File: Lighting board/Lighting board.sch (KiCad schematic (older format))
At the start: 16 parts, among them SW1 SW_SPDT, U1 LDD-1500L, U2 LDD-1500L, U3 TM4C129E_Launchpad, U4 OKI

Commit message: PDR commit
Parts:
- removed C2: 10uF, Capacitor_SMD:C_0603_1608Metric_Pad1.05x0.95mm_HandSolder, symbol Device:C
- removed Conn2C2: Molex_SL_03, MRDT_Connectors:MOLEX_SL_03_Vertical, symbol MRDT_Connectors:Molex_SL_03
- removed R2: 1k, Resistor_SMD:R_0603_1608Metric_Pad1.05x0.95mm_HandSolder, symbol Device:R
- Conn1C1, Conn1D1: footprint MRDT_Connectors:MOLEX_SL_02_Vertical -> MRDT_Connectors:MOLEX_SL_02_Horizontal
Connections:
- net labels removed: Dout_NeoPixel2, Dout_NeoPxiel2
- wire segments 35 -> 31
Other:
- note removed: "SPI MOSI(1)"
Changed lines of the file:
@@
 F 0 "Conn1C1" H 3377 4508 60  0000 L CNN
 F 1 "Molex_SL_02" H 3377 4402 60  0000 L CNN
-F 2 "MRDT_Connectors:MOLEX_SL_02_Vertical" H 3250 4250 60  0001 C CNN
+F 2 "MRDT_Connectors:MOLEX_SL_02_Horizontal" H 3250 4250 60  0001 C CNN
 F 3 "" H 3250 4250 60  0001 C CNN
 	1    3250 4350
@@
 F 0 "Conn1D1" H 3377 5458 60  0000 L CNN
 F 1 "Molex_SL_02" H 3377 5352 60  0000 L CNN
-F 2 "MRDT_Connectors:MOLEX_SL_02_Vertical" H 3250 5200 60  0001 C CNN
+F 2 "MRDT_Connectors:MOLEX_SL_02_Horizontal" H 3250 5200 60  0001 C CNN
 F 3 "" H 3250 5200 60  0001 C CNN
 	1    3250 5300
@@
 Text GLabel 1700 5450 0    50   UnSpc ~ 0
 GND
-Text GLabel 7950 2000 2    50   Output ~ 0
-Dout_NeoPxiel2
-Text Notes 8550 2150 2    50   ~ 0
-SPI MOSI(1)
 Wire Notes Line
 	8850 1650 8850 2950
@@
 Wire Wire Line
 	5800 4950 5650 4950
-Text GLabel 6350 5850 0    50   UnSpc ~ 0
-GND
-$Comp
-L Device:C C2
-U 1 1 5BD0A00B
-P 5500 5500
-F 0 "C2" H 5615 5546 50  0000 L CNN
-F 1 "10uF" H 5615 5455 50  0000 L CNN
-F 2 "Capacitor_SMD:C_0603_1608Metric_Pad1.05x0.95mm_HandSolder" H 5538 5350 50  0001 C CNN
-F 3 "~" H 5500 5500 50  0001 C CNN
-	1    5500 5500
-	0    -1   -1   0
-$EndComp
-Text GLabel 5350 5500 0    50   Input ~ 0
-5V
-Text GLabel 5650 5950 0    50   Input ~ 0
-Dout_NeoPixel2
-$Comp
-L MRDT_Connectors:Molex_SL_03 Conn2C2
-U 1 1 5BD0A013
-P 6550 6000
-F 0 "Conn2C2" H 6677 6208 60  0000 L CNN
-F 1 "Molex_SL_03" H 6677 6102 60  0000 L CNN
-F 2 "MRDT_Connectors:MOLEX_SL_03_Vertical" H 6550 6000 60  0001 C CNN
-F 3 "" H 6550 6000 60  0001 C CNN
-	1    6550 6000
-	1    0    0    -1
-$EndComp
-Wire Wire Line
-	6350 5750 6350 5500
-Wire Wire Line
-	5650 5500 6350 5500
-$Comp
-L Device:R R2
-U 1 1 5BD0A01B
-P 5950 5950
-F 0 "R2" V 5743 5950 50  0000 C CNN
-F 1 "1k" V 5834 5950 50  0000 C CNN
-F 2 "Resistor_SMD:R_0603_1608Metric_Pad1.05x0.95mm_HandSolder" V 5880 5950 50  0001 C CNN
-F 3 "~" H 5950 5950 50  0001 C CNN
-	1    5950 5950
-	0    1    1    0
-$EndComp
-Wire Wire Line
-	6100 5950 6350 5950
-Wire Wire Line
-	5800 5950 5650 5950
-Wire Notes Line
-	7550 6150 4900 6150
-Wire Notes Line
-	4900 6150 4900 4150
 Wire Notes Line
 	4900 4150 7550 4150
-Wire Notes Line
-	7550 4150 7550 6150
 Wire Wire Line
 	1700 5000 1700 5100
 Text GLabel 9500 5650 0    50   Input ~ 0
 V+Act
+Wire Notes Line
+	4900 4150 4900 5150
+Wire Notes Line
+	7550 4150 7550 5150
+Wire Notes Line
+	4900 5150 7550 5150
 $EndSCHEMATC

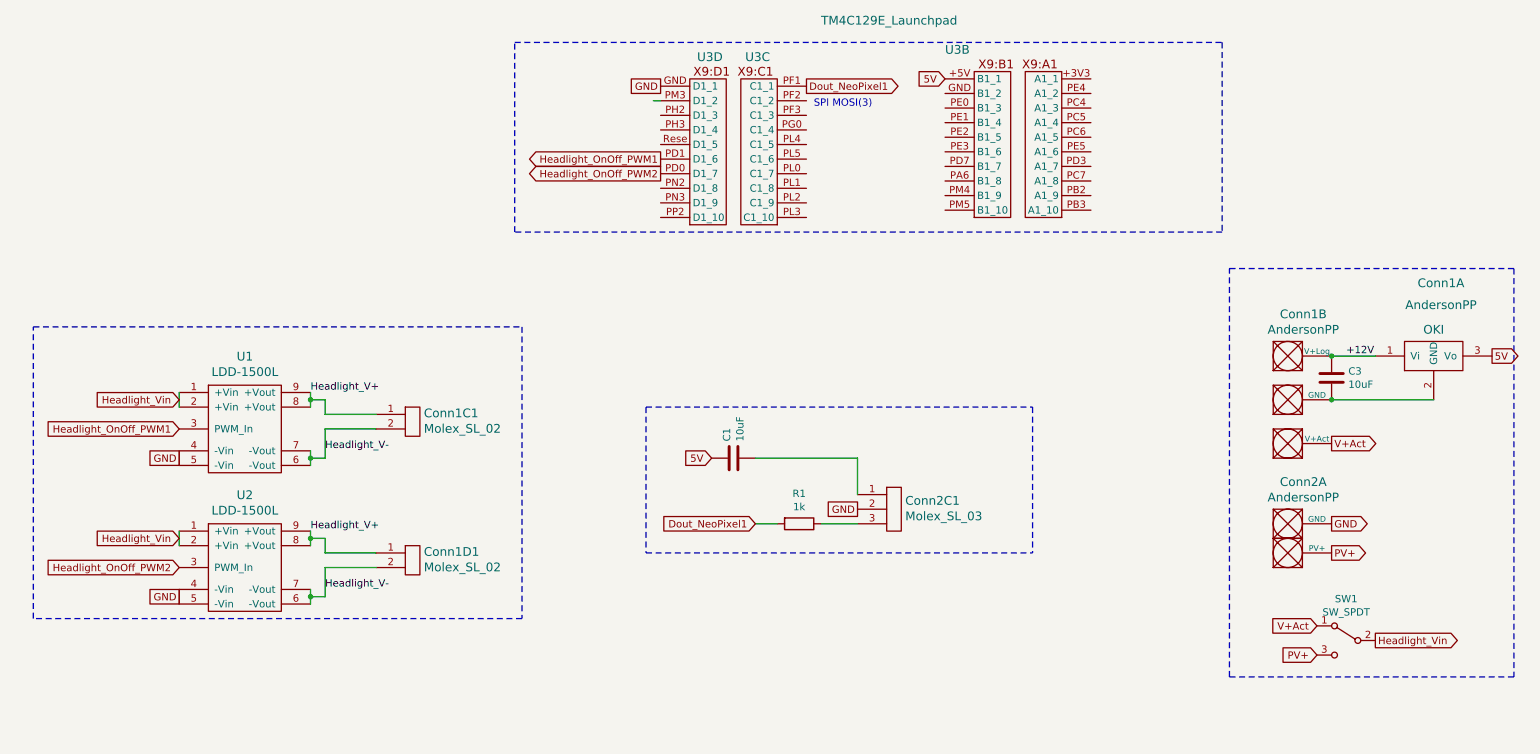
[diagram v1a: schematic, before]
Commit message: Changes 11/3
changed oki to AP1059 and started traces
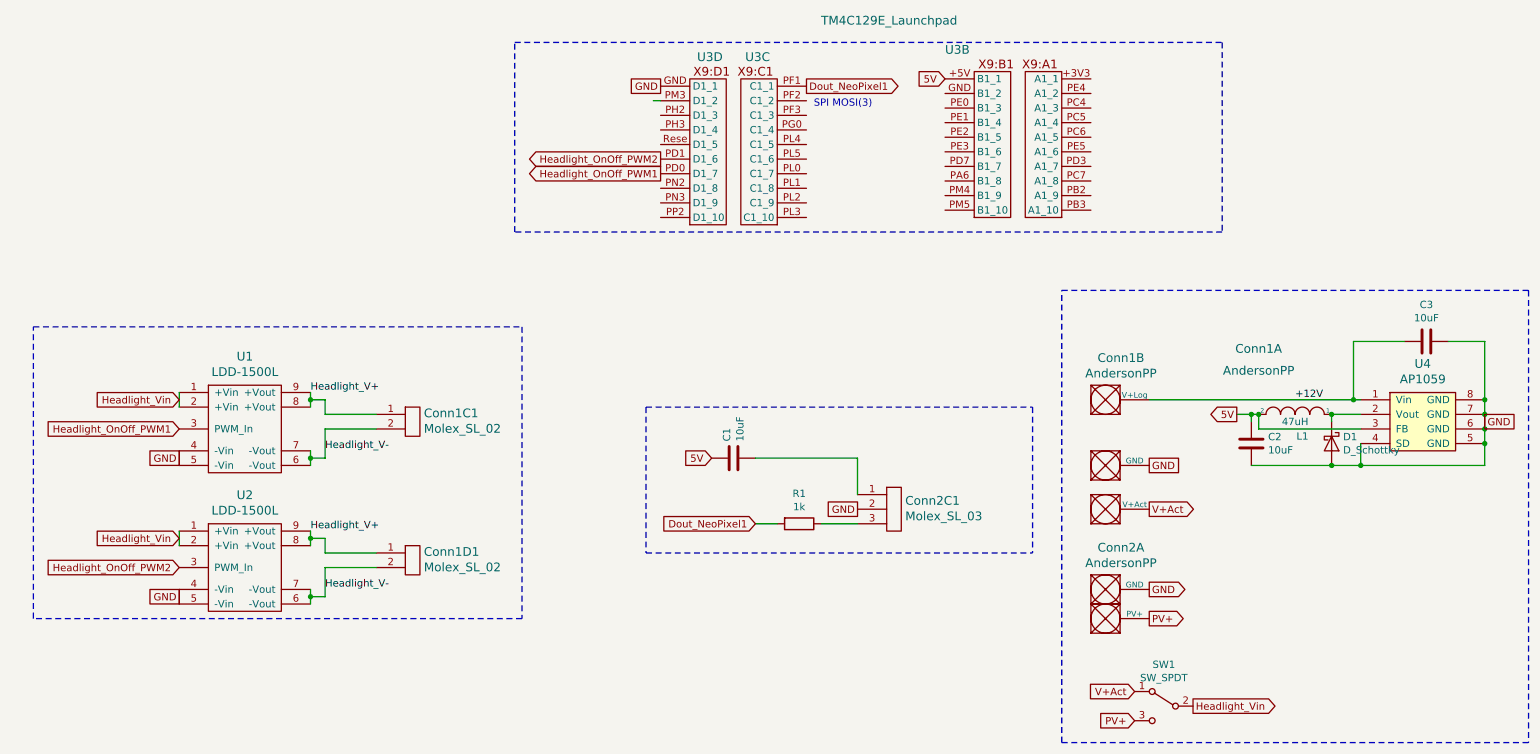
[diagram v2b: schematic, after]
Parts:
- removed U4: OKI, MRDT_Devices:OKI_Horizontal, symbol MRDT_Devices:OKI
- added C2: 10uF, Capacitor_SMD:C_0603_1608Metric_Pad1.05x0.95mm_HandSolder, symbol Device:C
- added D1: D_Schottky, Diode_SMD:D_0603_1608Metric_Pad1.05x0.95mm_HandSolder, symbol Device:D_Schottky
- added L1: 47uH, Inductor_SMD:L_0603_1608Metric_Pad1.05x0.95mm_HandSolder, symbol pspice:INDUCTOR
- added U4: AP1059, Package_SO:SO-8_5.3x6.2mm_P1.27mm, symbol MRDT_ICs:AP1059
- Conn1: renamed from Conn2; footprint Project Library:Anderson_2_Vertical -> MRDT_Connectors:Anderson_3_Horisontal_Side_by_Side
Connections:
- wire segments 31 -> 50
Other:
- moved on the sheet: Conn1A, Conn1B, Conn2A, SW1
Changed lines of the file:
@@
 Text GLabel 5000 1950 0    50   UnSpc ~ 0
 GND
-$Comp
-L Device:C C3
-U 1 1 5BCE5020
-P 9600 3950
-F 0 "C3" H 9715 3996 50  0000 L CNN
-F 1 "10uF" H 9715 3905 50  0000 L CNN
-F 2 "Capacitor_SMD:C_0603_1608Metric_Pad1.05x0.95mm_HandSolder" H 9638 3800 50  0001 C CNN
-F 3 "~" H 9600 3950 50  0001 C CNN
-	1    9600 3950
-	1    0    0    -1
-$EndComp
-$Comp
-L MRDT_Devices:OKI U4
-U 1 1 5BCFD699
-P 10100 3900
-F 0 "U4" H 10150 3850 60  0001 C CNN
-F 1 "OKI" H 10300 4181 60  0000 C CNN
-F 2 "MRDT_Devices:OKI_Horizontal" H 9900 3800 60  0001 C CNN
-F 3 "" H 9900 3800 60  0001 C CNN
-	1    10100 3900
-	1    0    0    -1
-$EndComp
-Text GLabel 10700 3800 2    50   Output ~ 0
-5V
 Text GLabel 6350 4850 0    50   UnSpc ~ 0
 GND
@@
 L MRDT_Connectors:AndersonPP Conn1
 U 1 1 5BCFE2EB
-P 9200 4200
-F 0 "Conn1" H 10350 5100 60  0000 C CNN
-F 1 "AndersonPP" H 10350 4950 60  0000 C CNN
-F 2 "MRDT_Connectors:Anderson_3_Horisontal_Side_by_Side" H 9050 3650 60  0001 C CNN
-F 3 "" H 9050 3650 60  0001 C CNN
-	1    9200 4200
+P 7950 4650
+F 0 "Conn1" H 9100 5550 60  0000 C CNN
+F 1 "AndersonPP" H 9100 5400 60  0000 C CNN
+F 2 "MRDT_Connectors:Anderson_3_Horisontal_Side_by_Side" H 7800 4100 60  0001 C CNN
+F 3 "" H 7800 4100 60  0001 C CNN
+	1    7950 4650
 	1    0    0    -1
 $EndComp
@@
 L MRDT_Connectors:AndersonPP Conn1
 U 2 1 5BCFE2A3
-P 9200 3900
-F 0 "Conn1" H 9406 4287 60  0000 C CNN
-F 1 "AndersonPP" H 9406 4181 60  0000 C CNN
-F 2 "MRDT_Connectors:Anderson_3_Horisontal_Side_by_Side" H 9050 3350 60  0001 C CNN
-F 3 "" H 9050 3350 60  0001 C CNN
-	2    9200 3900
-	1    0    0    -1
-$EndComp
-Wire Wire Line
-	9600 3800 9900 3800
-Connection ~ 9600 3800
-Wire Wire Line
-	9600 4100 10300 4100
-Connection ~ 9600 4100
+P 7950 4200
+F 0 "Conn1" H 8156 4587 60  0000 C CNN
+F 1 "AndersonPP" H 8156 4481 60  0000 C CNN
+F 2 "MRDT_Connectors:Anderson_3_Horisontal_Side_by_Side" H 7800 3650 60  0001 C CNN
+F 3 "" H 7800 3650 60  0001 C CNN
+	2    7950 4200
+	1    0    0    -1
+$EndComp
 $Comp
 L MRDT_Shields:TM4C129E_Launchpad U3
@@
 L MRDT_Connectors:AndersonPP Conn1
 U 3 1 5BCFEF35
-P 9200 4500
-F 0 "Conn1" H 9406 4887 60  0001 C CNN
-F 1 "AndersonPP" H 9406 4781 60  0001 C CNN
-F 2 "MRDT_Connectors:Anderson_3_Horisontal_Side_by_Side" H 9050 3950 60  0001 C CNN
-F 3 "" H 9050 3950 60  0001 C CNN
-	3    9200 4500
-	1    0    0    -1
-$EndComp
-$Comp
-L MRDT_Connectors:AndersonPP Conn2
+P 7950 4950
+F 0 "Conn1" H 8156 5337 60  0001 C CNN
+F 1 "AndersonPP" H 8156 5231 60  0001 C CNN
+F 2 "MRDT_Connectors:Anderson_3_Horisontal_Side_by_Side" H 7800 4400 60  0001 C CNN
+F 3 "" H 7800 4400 60  0001 C CNN
+	3    7950 4950
+	1    0    0    -1
+$EndComp
+$Comp
+L MRDT_Connectors:AndersonPP Conn1
 U 4 1 5BCFEFB2
-P 9200 5250
-F 0 "Conn2" H 9406 5637 60  0001 C CNN
-F 1 "AndersonPP" H 9406 5531 60  0001 C CNN
-F 2 "Project Library:Anderson_2_Vertical" H 9050 4700 60  0001 C CNN
-F 3 "" H 9050 4700 60  0001 C CNN
-	4    9200 5250
+P 7950 5700
+F 0 "Conn1" H 8156 6087 60  0001 C CNN
+F 1 "AndersonPP" H 8156 5981 60  0001 C CNN
+F 2 "MRDT_Connectors:Anderson_3_Horisontal_Side_by_Side" H 7800 5150 60  0001 C CNN
+F 3 "" H 7800 5150 60  0001 C CNN
+	4    7950 5700
 	1    0    0    -1
 $EndComp
@@
 L Switch:SW_SPDT SW1
 U 1 1 5BCFFE8E
-P 9700 5750
-F 0 "SW1" H 9700 6035 50  0000 C CNN
-F 1 "SW_SPDT" H 9700 5944 50  0000 C CNN
-F 2 "MRDT_Switches:1P2T_Angled_Slide_GPI-152-3013" H 9700 5750 50  0001 C CNN
-F 3 "" H 9700 5750 50  0001 C CNN
-	1    9700 5750
+P 8450 6200
+F 0 "SW1" H 8450 6485 50  0000 C CNN
+F 1 "SW_SPDT" H 8450 6394 50  0000 C CNN
+F 2 "MRDT_Switches:1P2T_Angled_Slide_GPI-152-3013" H 8450 6200 50  0001 C CNN
+F 3 "" H 8450 6200 50  0001 C CNN
+	1    8450 6200
 	-1   0    0    -1
 $EndComp
-Text GLabel 5000 2450 0    50   Output ~ 0
+Text GLabel 5000 2550 0    50   Output ~ 0
 Headlight_OnOff_PWM1
 Text Notes 6050 2100 0    50   ~ 0
@@
 Wire Wire Line
 	5000 2050 4950 2050
-Text Label 9700 3800 0    50   ~ 0
+Text Label 9350 4100 0    50   ~ 0
 +12V
 Wire Wire Line
@@
 L MRDT_Connectors:AndersonPP Conn2
 U 1 1 5BD01BD2
-P 9200 5050
-F 0 "Conn2" H 9406 5437 60  0000 C CNN
-F 1 "AndersonPP" H 9406 5331 60  0000 C CNN
-F 2 "Project Library:Anderson_2_Vertical" H 9050 4500 60  0001 C CNN
-F 3 "" H 9050 4500 60  0001 C CNN
-	1    9200 5050
-	1    0    0    -1
-$EndComp
-Text GLabel 9600 4400 2    50   Output ~ 0
+P 7950 5500
+F 0 "Conn2" H 8156 5887 60  0000 C CNN
+F 1 "AndersonPP" H 8156 5781 60  0000 C CNN
+F 2 "Project Library:Anderson_2_Vertical" H 7800 4950 60  0001 C CNN
+F 3 "" H 7800 4950 60  0001 C CNN
+	1    7950 5500
+	1    0    0    -1
+$EndComp
+Text GLabel 8350 4850 2    50   Output ~ 0
 V+Act
-Text GLabel 9600 4950 2    50   Output ~ 0
-GND
-Text GLabel 9600 5150 2    50   Output ~ 0
+Text GLabel 8350 5400 2    50   Output ~ 0
+GND
+Text GLabel 8350 5600 2    50   Output ~ 0
 PV+
-Text GLabel 9500 5850 0    50   Input ~ 0
+Text GLabel 8250 6300 0    50   Input ~ 0
 PV+
-Text GLabel 9900 5750 2    50   Output ~ 0
+Text GLabel 8650 6200 2    50   Output ~ 0
 Headlight_Vin
 Text GLabel 1700 4100 0    50   Input ~ 0
@@
 Wire Wire Line
 	2600 5050 2600 5100
-Text GLabel 5000 2550 0    50   Output ~ 0
+Text GLabel 5000 2450 0    50   Output ~ 0
 Headlight_OnOff_PWM2
 Wire Wire Line
@@
 Wire Notes Line
 	4050 5600 700  5600
-Wire Notes Line
-	8900 6000 8900 3200
-Wire Notes Line
-	8900 3200 10850 3200
-Wire Notes Line
-	10850 3200 10850 6000
-Wire Notes Line
-	10850 6000 8900 6000
 $Comp
 L Device:R R1
@@
 Wire Wire Line
 	1700 5000 1700 5100
-Text GLabel 9500 5650 0    50   Input ~ 0
+Text GLabel 8250 6100 0    50   Input ~ 0
 V+Act
 Wire Notes Line
@@
 Wire Notes Line
 	4900 5150 7550 5150
+$Comp
+L MRDT_ICs:AP1059 U4
+U 1 1 5BDE0F64
+P 10000 4450
+F 0 "U4" H 10225 5047 60  0000 C CNN
+F 1 "AP1059" H 10225 4941 60  0000 C CNN
+F 2 "Package_SO:SO-8_5.3x6.2mm_P1.27mm" H 9750 4350 60  0001 C CNN
+F 3 "" H 9750 4350 60  0001 C CNN
+	1    10000 4450
+	1    0    0    -1
+$EndComp
+Wire Wire Line
+	10650 4100 10650 4200
+Connection ~ 10650 4200
+Wire Wire Line
+	10650 4200 10650 4300
+Connection ~ 10650 4300
+Wire Wire Line
+	10650 4300 10650 4400
+Text GLabel 10650 4250 2    50   UnSpc ~ 0
+GND
+Wire Wire Line
+	9800 4400 9800 4550
+Wire Wire Line
+	9800 4550 10650 4550
+Wire Wire Line
+	10650 4550 10650 4400
+Connection ~ 10650 4400
+$Comp
+L Device:C C2
+U 1 1 5BDE3ABA
+P 9050 4400
+F 0 "C2" H 9165 4446 50  0000 L CNN
+F 1 "10uF" H 9165 4355 50  0000 L CNN
+F 2 "Capacitor_SMD:C_0603_1608Metric_Pad1.05x0.95mm_HandSolder" H 9088 4250 50  0001 C CNN
+F 3 "~" H 9050 4400 50  0001 C CNN
+	1    9050 4400
+	1    0    0    -1
+$EndComp
+$Comp
+L Device:D_Schottky D1
+U 1 1 5BDE4886
+P 9600 4400
+F 0 "D1" V 9554 4479 50  0000 L CNN
+F 1 "D_Schottky" V 9645 4479 50  0000 L CNN
+F 2 "Diode_SMD:D_0603_1608Metric_Pad1.05x0.95mm_HandSolder" H 9600 4400 50  0001 C CNN
+F 3 "~" H 9600 4400 50  0001 C CNN
+	1    9600 4400
+	0    1    1    0
+$EndComp
+Wire Wire Line
+	9600 4550 9800 4550
+Connection ~ 9800 4550
+Wire Wire Line
+	9600 4250 9600 4200
+Wire Wire Line
+	9600 4200 9800 4200
+$Comp
+L pspice:INDUCTOR L1
+U 1 1 5BDE5512
+P 9350 4200
+F 0 "L1" H 9300 4050 50  0000 C CNN
+F 1 "47uH" H 9350 4150 50  0000 C CNN
+F 2 "Inductor_SMD:L_0603_1608Metric_Pad1.05x0.95mm_HandSolder" H 9350 4200 50  0001 C CNN
+F 3 "~" H 9350 4200 50  0001 C CNN
+	1    9350 4200
+	-1   0    0    -1
+$EndComp
+Wire Wire Line
+	8350 4100 9750 4100
+Connection ~ 9600 4200
+Wire Wire Line
+	9800 4300 9100 4300
+Wire Wire Line
+	9100 4300 9100 4200
+Wire Wire Line
+	9100 4200 9050 4200
+Connection ~ 9100 4200
+Text GLabel 8950 4200 0    50   Output ~ 0
+5V
+Connection ~ 9050 4200
+Wire Wire Line
+	9050 4200 8950 4200
+Wire Wire Line
+	9050 4250 9050 4200
+Wire Wire Line
+	9050 4550 9600 4550
+Connection ~ 9600 4550
+Text GLabel 8350 4550 2    50   UnSpc ~ 0
+GND
+$Comp
+L Device:C C3
+U 1 1 5BDE8642
+P 10250 3700
+F 0 "C3" V 9998 3700 50  0000 C CNN
+F 1 "10uF" V 10089 3700 50  0000 C CNN
+F 2 "Capacitor_SMD:C_0603_1608Metric_Pad1.05x0.95mm_HandSolder" H 10288 3550 50  0001 C CNN
+F 3 "~" H 10250 3700 50  0001 C CNN
+	1    10250 3700
+	0    1    1    0
+$EndComp
+Wire Wire Line
+	9750 4100 9750 3700
+Wire Wire Line
+	9750 3700 10100 3700
+Connection ~ 9750 4100
+Wire Wire Line
+	9750 4100 9800 4100
+Wire Wire Line
+	10400 3700 10650 3700
+Wire Wire Line
+	10650 3700 10650 4100
+Connection ~ 10650 4100
+Wire Notes Line
+	7750 6450 7750 3350
+Wire Notes Line
+	7750 3350 10950 3350
+Wire Notes Line
+	10950 3350 10950 6450
+Wire Notes Line
+	10950 6450 7750 6450
 $EndSCHEMATC
